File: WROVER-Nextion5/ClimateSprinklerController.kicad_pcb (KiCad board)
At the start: 2 copper layers, 169.5 x 84 mm, 184 parts, among them J1 7.5 TO 40 V, J10 HVAC, J2 USB_B_Micro, J3 POWER_SEL, J4 NEXTION, J5 SERIAL, J6 SPI, J7 PIR, J8 I2C, J9 IO_EXP, K1 G6E-134P-US DC5, Q1 MMSS8050, Q2 MMSS8050, Q3 TEPT5700, Q4 2N7002, Q5 2N6073B, Q6 2N6073B, Q7 2N6073B, Q8 2N6073B, Q9 2N6073B, SW1 POWER, SW2 RESET, SW3 MODE, U1 ESP32-WROVER, U10 SHTC3, U11 TMP117, U12 MOC3043, U13 MOC3043, U14 MOC3043, U15 MOC3043, U16 MOC3043, U17 DHT22, U2 MCP23017_SO, U3 FT232RL, U4 TPS22917DBV, U5 LMR36520, U6 SGP40-Sensor_Air_Quality, U7 BME680, U8 LD1086DT33TR, U9 BME280

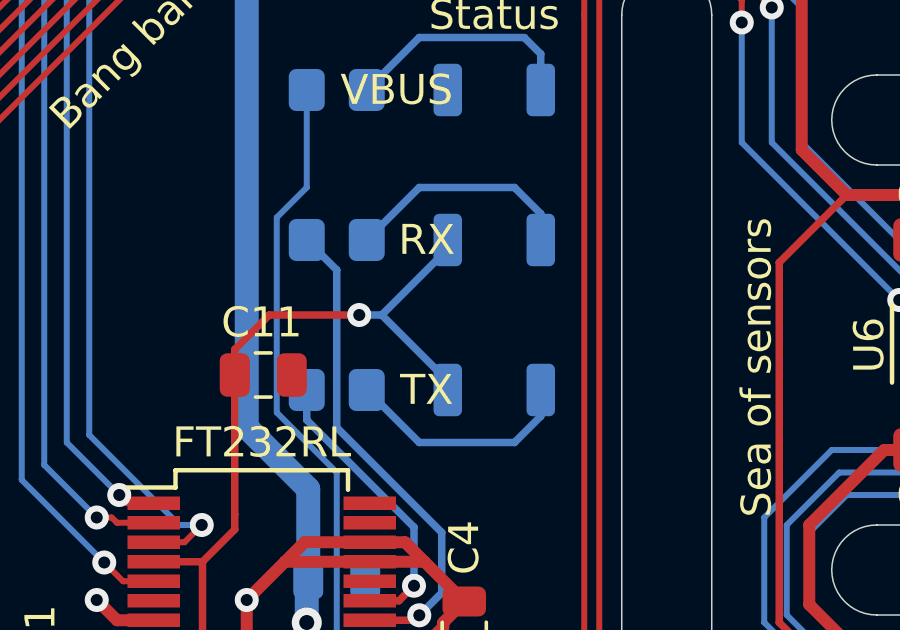
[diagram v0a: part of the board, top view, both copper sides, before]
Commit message: TX+RX LEDs were backwards...oops
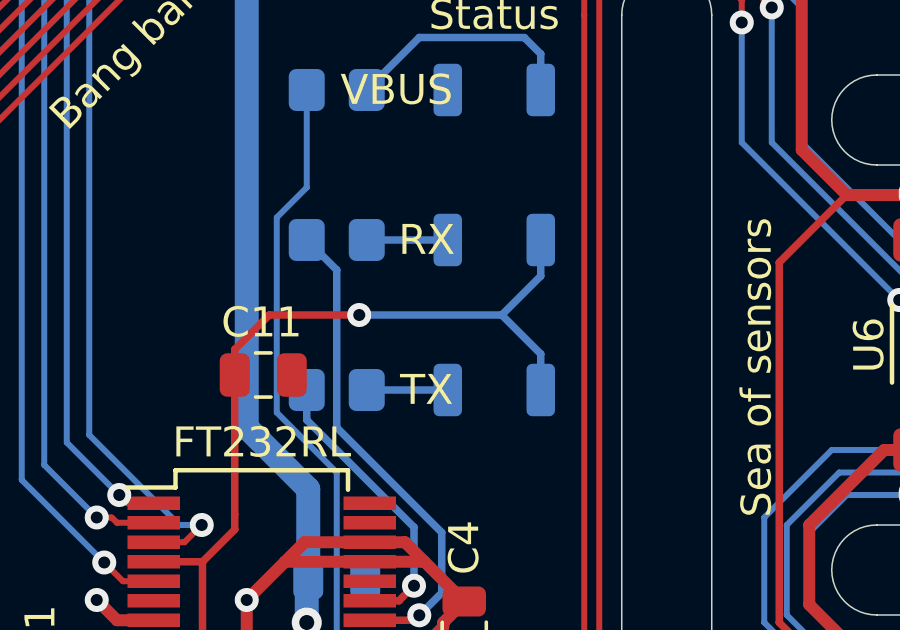
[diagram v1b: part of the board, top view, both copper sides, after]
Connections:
- D3 pad 1: Net-(C11-Pad1) -> Net-(D3-Pad1)
- D3 pad 2: Net-(D3-Pad2) -> Net-(C11-Pad1)
- D4 pad 1: Net-(C11-Pad1) -> Net-(D4-Pad1)
- D4 pad 2: Net-(D4-Pad2) -> Net-(C11-Pad1)
- R10 pad 1: Net-(D4-Pad2) -> Net-(D4-Pad1)
- R9 pad 1: Net-(D3-Pad2) -> Net-(D3-Pad1)
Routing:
- net Net-(D4-Pad2): track 7.76 -> 0.00 mm
- net Net-(D3-Pad2): track 7.76 -> 0.00 mm
- net Net-(C11-Pad1): track 38.9 -> 42.2 mm
- net Net-(D4-Pad1): track 0.00 -> 2.70 mm
- net Net-(D3-Pad1): track 0.00 -> 2.70 mm

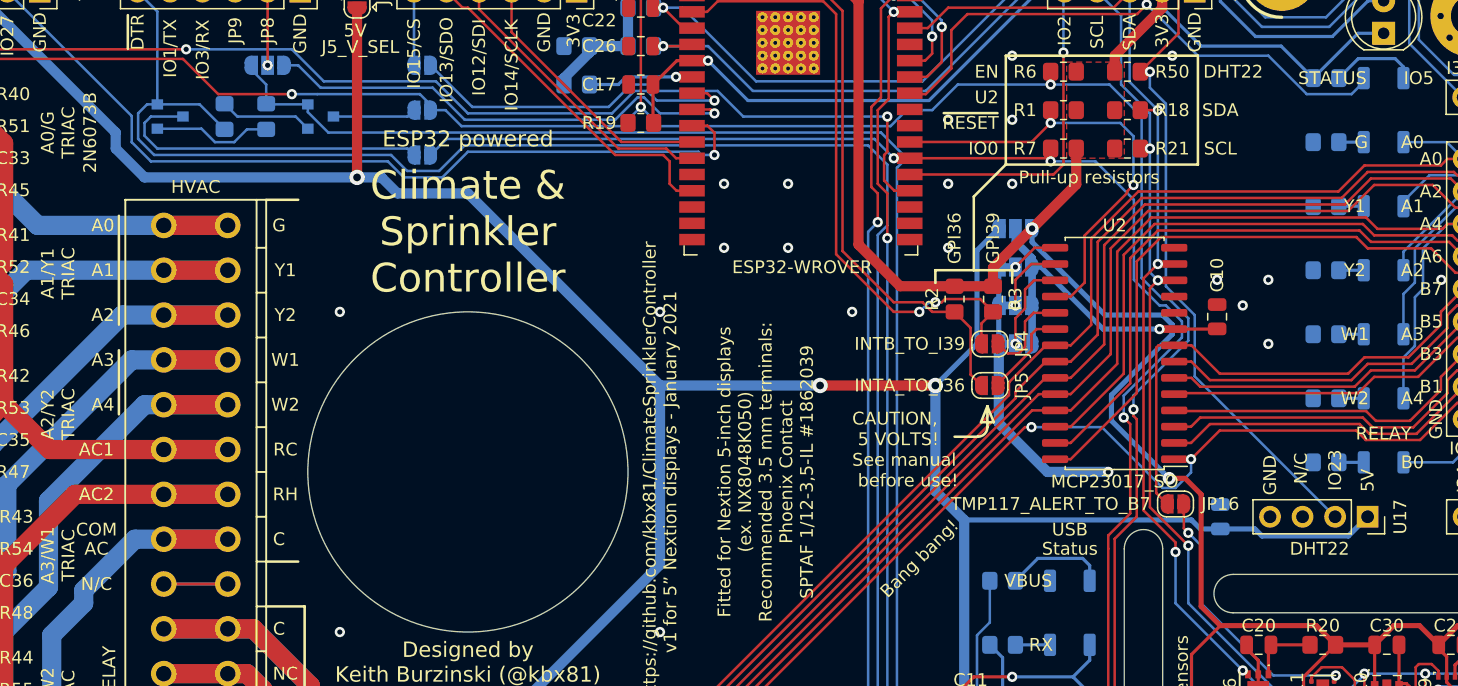
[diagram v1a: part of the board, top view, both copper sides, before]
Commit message: Doc updates, new images, new enclosures, regenerate gerbers
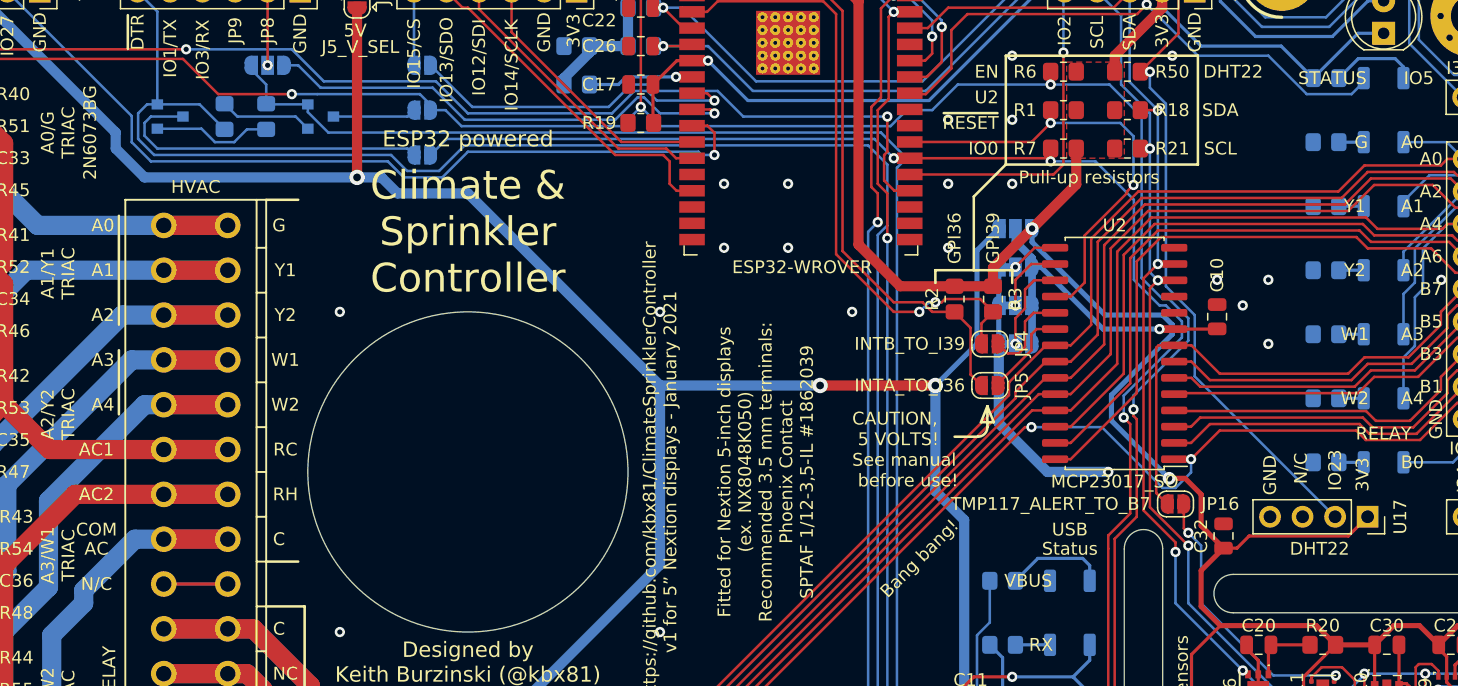
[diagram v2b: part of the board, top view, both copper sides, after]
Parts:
- C32: moved to F.Cu
- D1: value MBR230S1F-7 -> N/A
- D2: value CD-MBL206SL -> N/A
- D9: value 1N4148 -> N/A
- J2: value USB_B_Micro -> N/A
- Q5, Q6, Q7, Q8, Q9: value 2N6073B -> 2N6073BG
- R29: value 1K2 -> 560
- R31, R32: value 1K2 -> 1K5
- RV1: value B72205S0400K101 -> N/A
- TH1, TH2: value NXFT15XH103FA2B100 -> 10K
- U6: value SGP40-Sensor_Air_Quality -> SGP40
- moved C32 1.52 mm to (209.0, 95.0)
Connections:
- C32 pad 1: +5V -> +3V3
- U17 pad 1: +5V -> +3V3
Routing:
- net +5V: track 352.4 -> 319.8 mm
- net +3V3: track 339.3 -> 353.0 mm
